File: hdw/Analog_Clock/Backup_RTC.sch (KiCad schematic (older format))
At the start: 4 parts

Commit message: More schematic work
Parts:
- added BT?: CR2032, symbol Device:Battery_Cell
- added BT?: CR2032_Holder, Battery_Holders:Keystone_1058_1x2032-CoinCell, symbol Device:Battery_Cell
- added U?: MIC845N, Package_TO_SOT_SMD:SOT-353_SC-70-5, symbol Comparator:MIC845N
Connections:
- no-connect marks 3 -> 5
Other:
- note added: "REPLACE WITH SOMETHING SIMILAR"
- moved on the sheet: C?, U?
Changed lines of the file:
@@
 EESchema Schematic File Version 4
+LIBS:Analog_Clock-cache
 EELAYER 30 0
 EELAYER END
@@
 L Timer_RTC:DS3231MZ U?
 U 1 1 5E217505
-P 5420 3530
-F 0 "U?" H 5120 3880 50  0000 R CNN
-F 1 "DS3231MZ" H 5870 3880 50  0000 R CNN
-F 2 "Package_SO:SOIC-8_3.9x4.9mm_P1.27mm" H 5420 3030 50  0001 C CNN
-F 3 "http://datasheets.maximintegrated.com/en/ds/DS3231M.pdf" H 5420 2930 50  0001 C CNN
-F 4 "DS3231MZ+-ND" H 5420 3530 50  0001 C CNN "Digi-Key PN"
-	1    5420 3530
+P 5400 2620
+F 0 "U?" H 5100 2970 50  0000 R CNN
+F 1 "DS3231MZ" H 5850 2970 50  0000 R CNN
+F 2 "Package_SO:SOIC-8_3.9x4.9mm_P1.27mm" H 5400 2120 50  0001 C CNN
+F 3 "http://datasheets.maximintegrated.com/en/ds/DS3231M.pdf" H 5400 2020 50  0001 C CNN
+F 4 "DS3231MZ+-ND" H 5400 2620 50  0001 C CNN "Digi-Key PN"
+	1    5400 2620
 	1    0    0    -1
 $EndComp
@@
 L power:GND #PWR?
 U 1 1 5E217898
-P 5420 3930
-F 0 "#PWR?" H 5420 3680 50  0001 C CNN
-F 1 "GND" H 5420 3780 50  0000 C CNN
-F 2 "" H 5420 3930 50  0001 C CNN
-F 3 "" H 5420 3930 50  0001 C CNN
-	1    5420 3930
+P 5400 3020
+F 0 "#PWR?" H 5400 2770 50  0001 C CNN
+F 1 "GND" H 5400 2870 50  0000 C CNN
+F 2 "" H 5400 3020 50  0001 C CNN
+F 3 "" H 5400 3020 50  0001 C CNN
+	1    5400 3020
 	1    0    0    -1
 $EndComp
@@
 L power:+3.3V #PWR?
 U 1 1 5E217DBC
-P 5420 3130
-F 0 "#PWR?" H 5420 2980 50  0001 C CNN
-F 1 "+3.3V" H 5500 3270 50  0000 C CNN
-F 2 "" H 5420 3130 50  0001 C CNN
-F 3 "" H 5420 3130 50  0001 C CNN
-	1    5420 3130
+P 5400 2220
+F 0 "#PWR?" H 5400 2070 50  0001 C CNN
+F 1 "+3.3V" H 5480 2360 50  0000 C CNN
+F 2 "" H 5400 2220 50  0001 C CNN
+F 3 "" H 5400 2220 50  0001 C CNN
+	1    5400 2220
 	1    0    0    -1
 $EndComp
@@
 L Custom_Library:VBAT #PWR?
 U 1 1 5E2180E2
-P 5320 3130
-F 0 "#PWR?" H 5320 2980 50  0001 C CNN
-F 1 "VBAT" H 5240 3270 50  0000 C CNN
-F 2 "" H 5320 3130 50  0001 C CNN
-F 3 "" H 5320 3130 50  0001 C CNN
-	1    5320 3130
-	1    0    0    -1
-$EndComp
-NoConn ~ 5920 3330
-NoConn ~ 5920 3630
-NoConn ~ 4920 3730
-Text GLabel 4920 3430 0    50   BiDi ~ 0
+P 5300 2220
+F 0 "#PWR?" H 5300 2070 50  0001 C CNN
+F 1 "VBAT" H 5220 2360 50  0000 C CNN
+F 2 "" H 5300 2220 50  0001 C CNN
+F 3 "" H 5300 2220 50  0001 C CNN
+	1    5300 2220
+	1    0    0    -1
+$EndComp
+NoConn ~ 5900 2420
+NoConn ~ 5900 2720
+NoConn ~ 4900 2820
+Text GLabel 4900 2520 0    50   BiDi ~ 0
 I2C_SDA
-Text GLabel 4920 3330 0    50   Input ~ 0
+Text GLabel 4900 2420 0    50   Input ~ 0
 I2C_SCL
 $Comp
 L Custom_Library:C_Custom C?
 U 1 1 5E21E9AC
-P 5840 4720
-F 0 "C?" H 5865 4820 50  0000 L CNN
-F 1 "0.1uF" H 5865 4620 50  0000 L CNN
-F 2 "Capacitors_SMD:C_0402" H 5878 4570 50  0001 C CNN
-F 3 "" H 5865 4820 50  0001 C CNN
-F 4 "0402" H 5690 4820 50  0000 R CNN "display_footprint"
-F 5 "50V" H 5690 4720 50  0000 R CNN "Voltage"
-F 6 "X7R" H 5690 4620 50  0000 R CNN "Dielectric"
-F 7 "490-10701-1-ND" H 5840 4720 50  0001 C CNN "Digi-Key PN"
-	1    5840 4720
+P 5820 3810
+F 0 "C?" H 5845 3910 50  0000 L CNN
+F 1 "0.1uF" H 5845 3710 50  0000 L CNN
+F 2 "Capacitors_SMD:C_0402" H 5858 3660 50  0001 C CNN
+F 3 "" H 5845 3910 50  0001 C CNN
+F 4 "0402" H 5670 3910 50  0000 R CNN "display_footprint"
+F 5 "50V" H 5670 3810 50  0000 R CNN "Voltage"
+F 6 "X7R" H 5670 3710 50  0000 R CNN "Dielectric"
+F 7 "490-10701-1-ND" H 5820 3810 50  0001 C CNN "Digi-Key PN"
+	1    5820 3810
 	1    0    0    -1
 $EndComp
@@
 L power:+3.3V #PWR?
 U 1 1 5E21E9B2
-P 5840 4570
-F 0 "#PWR?" H 5840 4420 50  0001 C CNN
-F 1 "+3.3V" H 5840 4710 50  0000 C CNN
-F 2 "" H 5840 4570 50  0000 C CNN
-F 3 "" H 5840 4570 50  0000 C CNN
-	1    5840 4570
+P 5820 3660
+F 0 "#PWR?" H 5820 3510 50  0001 C CNN
+F 1 "+3.3V" H 5820 3800 50  0000 C CNN
+F 2 "" H 5820 3660 50  0000 C CNN
+F 3 "" H 5820 3660 50  0000 C CNN
+	1    5820 3660
 	1    0    0    -1
 $EndComp
@@
 L power:GND #PWR?
 U 1 1 5E21E9B8
-P 5840 4870
-F 0 "#PWR?" H 5840 4620 50  0001 C CNN
-F 1 "GND" H 5840 4720 50  0000 C CNN
-F 2 "" H 5840 4870 50  0001 C CNN
-F 3 "" H 5840 4870 50  0001 C CNN
-	1    5840 4870
+P 5820 3960
+F 0 "#PWR?" H 5820 3710 50  0001 C CNN
+F 1 "GND" H 5820 3810 50  0000 C CNN
+F 2 "" H 5820 3960 50  0001 C CNN
+F 3 "" H 5820 3960 50  0001 C CNN
+	1    5820 3960
 	1    0    0    -1
 $EndComp
@@
 L Custom_Library:C_Custom C?
 U 1 1 5E220EDC
-P 5110 4720
-F 0 "C?" H 5135 4820 50  0000 L CNN
-F 1 "0.1uF" H 5135 4620 50  0000 L CNN
-F 2 "Capacitors_SMD:C_0402" H 5148 4570 50  0001 C CNN
-F 3 "" H 5135 4820 50  0001 C CNN
-F 4 "0402" H 4960 4820 50  0000 R CNN "display_footprint"
-F 5 "50V" H 4960 4720 50  0000 R CNN "Voltage"
-F 6 "X7R" H 4960 4620 50  0000 R CNN "Dielectric"
-F 7 "490-10701-1-ND" H 5110 4720 50  0001 C CNN "Digi-Key PN"
-	1    5110 4720
+P 5090 3810
+F 0 "C?" H 5115 3910 50  0000 L CNN
+F 1 "0.1uF" H 5115 3710 50  0000 L CNN
+F 2 "Capacitors_SMD:C_0402" H 5128 3660 50  0001 C CNN
+F 3 "" H 5115 3910 50  0001 C CNN
+F 4 "0402" H 4940 3910 50  0000 R CNN "display_footprint"
+F 5 "50V" H 4940 3810 50  0000 R CNN "Voltage"
+F 6 "X7R" H 4940 3710 50  0000 R CNN "Dielectric"
+F 7 "490-10701-1-ND" H 5090 3810 50  0001 C CNN "Digi-Key PN"
+	1    5090 3810
 	1    0    0    -1
 $EndComp
@@
 L power:GND #PWR?
 U 1 1 5E220EE8
-P 5110 4870
-F 0 "#PWR?" H 5110 4620 50  0001 C CNN
-F 1 "GND" H 5110 4720 50  0000 C CNN
-F 2 "" H 5110 4870 50  0001 C CNN
-F 3 "" H 5110 4870 50  0001 C CNN
-	1    5110 4870
+P 5090 3960
+F 0 "#PWR?" H 5090 3710 50  0001 C CNN
+F 1 "GND" H 5090 3810 50  0000 C CNN
+F 2 "" H 5090 3960 50  0001 C CNN
+F 3 "" H 5090 3960 50  0001 C CNN
+	1    5090 3960
 	1    0    0    -1
 $EndComp
@@
 L Custom_Library:VBAT #PWR?
 U 1 1 5E220F81
-P 5110 4570
-F 0 "#PWR?" H 5110 4420 50  0001 C CNN
-F 1 "VBAT" H 5110 4720 50  0000 C CNN
-F 2 "" H 5110 4570 50  0001 C CNN
-F 3 "" H 5110 4570 50  0001 C CNN
-	1    5110 4570
+P 5090 3660
+F 0 "#PWR?" H 5090 3510 50  0001 C CNN
+F 1 "VBAT" H 5090 3810 50  0000 C CNN
+F 2 "" H 5090 3660 50  0001 C CNN
+F 3 "" H 5090 3660 50  0001 C CNN
+	1    5090 3660
 	1    0    0    -1
 $EndComp
@@
 L Custom_Library:I2C_Address DOC?
 U 1 1 5E990E17
-P 7180 4080
-F 0 "DOC?" H 7180 4330 60  0001 C CNN
-F 1 "I2C_Address" H 6730 4080 60  0000 L CNN
-F 2 "" H 7180 4430 60  0001 C CNN
-F 3 "" H 7180 4430 60  0001 C CNN
-	1    7180 4080
-	1    0    0    -1
-$EndComp
+P 7160 3170
+F 0 "DOC?" H 7160 3420 60  0001 C CNN
+F 1 "I2C_Address" H 6710 3170 60  0000 L CNN
+F 2 "" H 7160 3520 60  0001 C CNN
+F 3 "" H 7160 3520 60  0001 C CNN
+	1    7160 3170
+	1    0    0    -1
+$EndComp
+$Comp
+L Device:Battery_Cell BT?
+U 1 1 5EA04714
+P 1840 5380
+F 0 "BT?" H 1940 5480 50  0000 L CNN
+F 1 "CR2032" H 1940 5380 50  0000 L CNN
+F 2 "" V 1840 5440 50  0001 C CNN
+F 3 "~" V 1840 5440 50  0001 C CNN
+F 4 "P189-ND" H 1840 5380 50  0001 C CNN "Digi-Key PN"
+	1    1840 5380
+	1    0    0    -1
+$EndComp
+NoConn ~ 1840 5480
+NoConn ~ 1840 5180
+$Comp
+L Device:Battery_Cell BT?
+U 1 1 5EA086C4
+P 2580 5380
+F 0 "BT?" H 2680 5480 50  0000 L CNN
+F 1 "CR2032_Holder" H 2680 5380 50  0000 L CNN
+F 2 "Battery_Holders:Keystone_1058_1x2032-CoinCell" V 2580 5440 50  0001 C CNN
+F 3 "~" V 2580 5440 50  0001 C CNN
+F 4 "36-1058-ND" H 2580 5380 50  0001 C CNN "Digi-Key PN"
+	1    2580 5380
+	1    0    0    -1
+$EndComp
+$Comp
+L power:GND #PWR?
+U 1 1 5EA0966C
+P 2580 5480
+F 0 "#PWR?" H 2580 5230 50  0001 C CNN
+F 1 "GND" H 2580 5330 50  0000 C CNN
+F 2 "" H 2580 5480 50  0001 C CNN
+F 3 "" H 2580 5480 50  0001 C CNN
+	1    2580 5480
+	1    0    0    -1
+$EndComp
+$Comp
+L Custom_Library:VBAT #PWR?
+U 1 1 5EA09B4F
+P 2580 5180
+F 0 "#PWR?" H 2580 5030 50  0001 C CNN
+F 1 "VBAT" H 2580 5330 50  0000 C CNN
+F 2 "" H 2580 5180 50  0001 C CNN
+F 3 "" H 2580 5180 50  0001 C CNN
+	1    2580 5180
+	1    0    0    -1
+$EndComp
+$Comp
+L Comparator:MIC845N U?
+U 1 1 5EA0D285
+P 6230 5620
+F 0 "U?" H 6380 5820 50  0000 C CNN
+F 1 "MIC845N" H 6530 5420 50  0000 C CNN
+F 2 "Package_TO_SOT_SMD:SOT-353_SC-70-5" H 6230 5620 50  0001 C CNN
+F 3 "http://ww1.microchip.com/downloads/en/DeviceDoc/mic845.pdf" H 6380 5820 50  0001 C CNN
+	1    6230 5620
+	1    0    0    -1
+$EndComp
+Text Notes 5780 5640 0    50   ~ 0
+REPLACE WITH SOMETHING SIMILAR
 $EndSCHEMATC

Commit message: More sch work
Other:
- note added: "Replace with smaller battery?"
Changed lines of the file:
@@
 $Descr A 11000 8500
 encoding utf-8
-Sheet 12 20
+Sheet 12 21
 Title ""
 Date ""
@@
 Text Notes 5780 5640 0    50   ~ 0
 REPLACE WITH SOMETHING SIMILAR
+Text Notes 1740 4520 0    100  ~ 20
+Replace with smaller battery?
 $EndSCHEMATC

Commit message: more sch progress
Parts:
- removed U?: MIC845N, Package_TO_SOT_SMD:SOT-353_SC-70-5, symbol Comparator:MIC845N
- added C?: 10uF, Capacitors_SMD:C_0402, symbol Custom_Library:C_Custom
- added R? (x3): 10k, Resistors_SMD:R_0402, symbol Custom_Library:R_Custom
- added R?: 105k, Resistors_SMD:R_0402, symbol Custom_Library:R_Custom
- added U?: TLV6700, TO_SOT_Packages_SMD:TSOT-23-6, symbol Custom_Library:TLV6700
- BT?: value CR2032 -> CR1616; Digi-Key PN P189-ND -> P034-ND
- BT?: value CR2032_Holder -> CR1616_Holder; footprint Battery_Holders:Keystone_1058_1x2032-CoinCell -> Custom Footprints Library:BAT_BU1632SM-JJ-GTR; Digi-Key PN 36-1058-ND -> BU1632SM-JJ-GCT-ND
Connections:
- net labels added: VBAT_PGOOD
- wire segments 0 -> 7
- no-connect marks 5 -> 6
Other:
- note added: "Falling threshold set to 2.5V"
- note removed: "REPLACE WITH SOMETHING SIMILAR"
- note removed: "Replace with smaller battery?"

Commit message: more analog work, added some more sch stuff
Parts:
- removed R? (x2): 10k, Resistors_SMD:R_0402, symbol Custom_Library:R_Custom
- added R?: 10k, Resistors_SMD:R_0402, symbol Custom_Library:R_Custom
- added R?: 22k, Resistors_SMD:R_0603, symbol Custom_Library:R_Custom
- added TP?: TP, Custom Footprints Library:Test_Point, symbol Custom_Library:TP
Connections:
- net GND: now also R?.2, R?.2
- net Backup_RTC_REFCLK: now reaches U?.1 (32KHZ)
- net Backup_RTC_REFCLK: now also R?.1, TP?.1 (TP)
- net at R?.2, U?.3 (+INA): now also R?.1
- no-connect marks 6 -> 5
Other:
- moved on the sheet: BT?, C?, R?, U?

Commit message: big sch push
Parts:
- added C1204, C1205: 0.1uF, Capacitors_SMD:C_0603, symbol Custom_Library:C_Custom
- added R1205, R1206: 562k, Resistors_SMD:R_0603, symbol Custom_Library:R_Custom
- added TP1201: TP, Custom Footprints Library:Test_Point, symbol Custom_Library:TP
- C1201: renamed from C?; footprint Capacitors_SMD:C_0402 -> Capacitors_SMD:C_0603; Digi-Key PN 490-13211-1-ND -> 490-10474-1-ND; Voltage 6.3V -> 10V; display_footprint 0402 -> 0603
- C1202, C1203: renamed from C?; footprint Capacitors_SMD:C_0402 -> Capacitors_SMD:C_0603; Digi-Key PN 490-10701-1-ND -> 399-7845-1-ND; display_footprint 0402 -> 0603
- DOC1201: renamed from DOC?; value I2C_Address -> 0x68
- R1201: renamed from R?; footprint Resistors_SMD:R_0402 -> Resistors_SMD:R_0603; Wattage 1/16W -> 1/10W; display_footprint 0402 -> 0603
- R1202: renamed from R?; Digi-Key PN A129704CT-ND -> (none)
- R1203, R1204: renamed from R?; footprint Resistors_SMD:R_0402 -> Resistors_SMD:R_0603; Digi-Key PN RMCF0402FT10K0CT-ND -> (none); Wattage 1/16W -> 1/10W; display_footprint 0402 -> 0603
- gave numbers to parts that had none: 5
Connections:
- net +3V3: now also C1204.1
- net GND: now also C1204.2, C1205.2, R1206.2
- net VBAT: now also R1205.1, TP1201.1 (TP)
- new net VBAT_ADC: C1205.1, R1205.2, R1206.1
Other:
- moved on the sheet: BT1201, BT1202, C1201, C1202, C1203, R1201, R1202, R1203, R1204, TP1202, U1201, U1202

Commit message: Much more schematic progress
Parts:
- R1201: Digi-Key PN (none) -> RMCF0603FT105KCT-ND
- R1202: Digi-Key PN (none) -> 311-22KLDCT-ND
- R1203, R1204: Digi-Key PN (none) -> YAG2321CT-ND
- R1205, R1206: Digi-Key PN (none) -> 311-562KHRCT-ND
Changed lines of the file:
@@
 encoding utf-8
 Sheet 12 25
-Title ""
-Date ""
-Rev ""
-Comp ""
+Title "Analog Clock"
+Date "2020-08-15"
+Rev "A"
+Comp "Drew Maatman"
 Comment1 ""
 Comment2 ""
@@
 F 5 "1%" H 4200 4390 50  0000 L CNN "Tolerance"
 F 6 "1/10W" H 4200 4320 50  0000 L CNN "Wattage"
+F 7 "RMCF0603FT105KCT-ND" H 4130 4390 50  0001 C CNN "Digi-Key PN"
 	1    4130 4390
 	-1   0    0    -1
@@
 F 5 "1%" H 6280 4390 50  0000 L CNN "Tolerance"
 F 6 "1/10W" H 6280 4320 50  0000 L CNN "Wattage"
-F 7 "" H 6210 4390 50  0001 C CNN "Digi-Key PN"
+F 7 "YAG2321CT-ND" H 6210 4390 50  0001 C CNN "Digi-Key PN"
 	1    6210 4390
 	-1   0    0    -1
@@
 F 5 "1%" H 7990 2030 50  0000 L CNN "Tolerance"
 F 6 "1/10W" H 7990 1960 50  0000 L CNN "Wattage"
-F 7 "" H 7920 2030 50  0001 C CNN "Digi-Key PN"
+F 7 "YAG2321CT-ND" H 7920 2030 50  0001 C CNN "Digi-Key PN"
 	1    7920 2030
 	-1   0    0    -1
@@
 F 5 "1%" H 4200 4810 50  0000 L CNN "Tolerance"
 F 6 "1/10W" H 4200 4720 50  0000 L CNN "Wattage"
-F 7 "" H 4430 5250 60  0001 C CNN "Digi-Key PN"
+F 7 "311-22KLDCT-ND" H 4430 5250 60  0001 C CNN "Digi-Key PN"
 	1    4130 4850
 	-1   0    0    -1
@@
 F 5 "1%" H 8040 4470 50  0000 L CNN "Tolerance"
 F 6 "1/10W" H 8050 4390 50  0000 L CNN "Wattage"
-F 7 "" H 7940 4470 50  0001 C CNN "Digi-Key PN"
+F 7 "311-562KHRCT-ND" H 7940 4470 50  0001 C CNN "Digi-Key PN"
 	1    7940 4470
 	1    0    0    -1
@@
 F 5 "1%" H 8040 4930 50  0000 L CNN "Tolerance"
 F 6 "1/10W" H 8050 4850 50  0000 L CNN "Wattage"
-F 7 "" H 7940 4930 50  0001 C CNN "Digi-Key PN"
+F 7 "311-562KHRCT-ND" H 7940 4930 50  0001 C CNN "Digi-Key PN"
 	1    7940 4930
 	1    0    0    -1

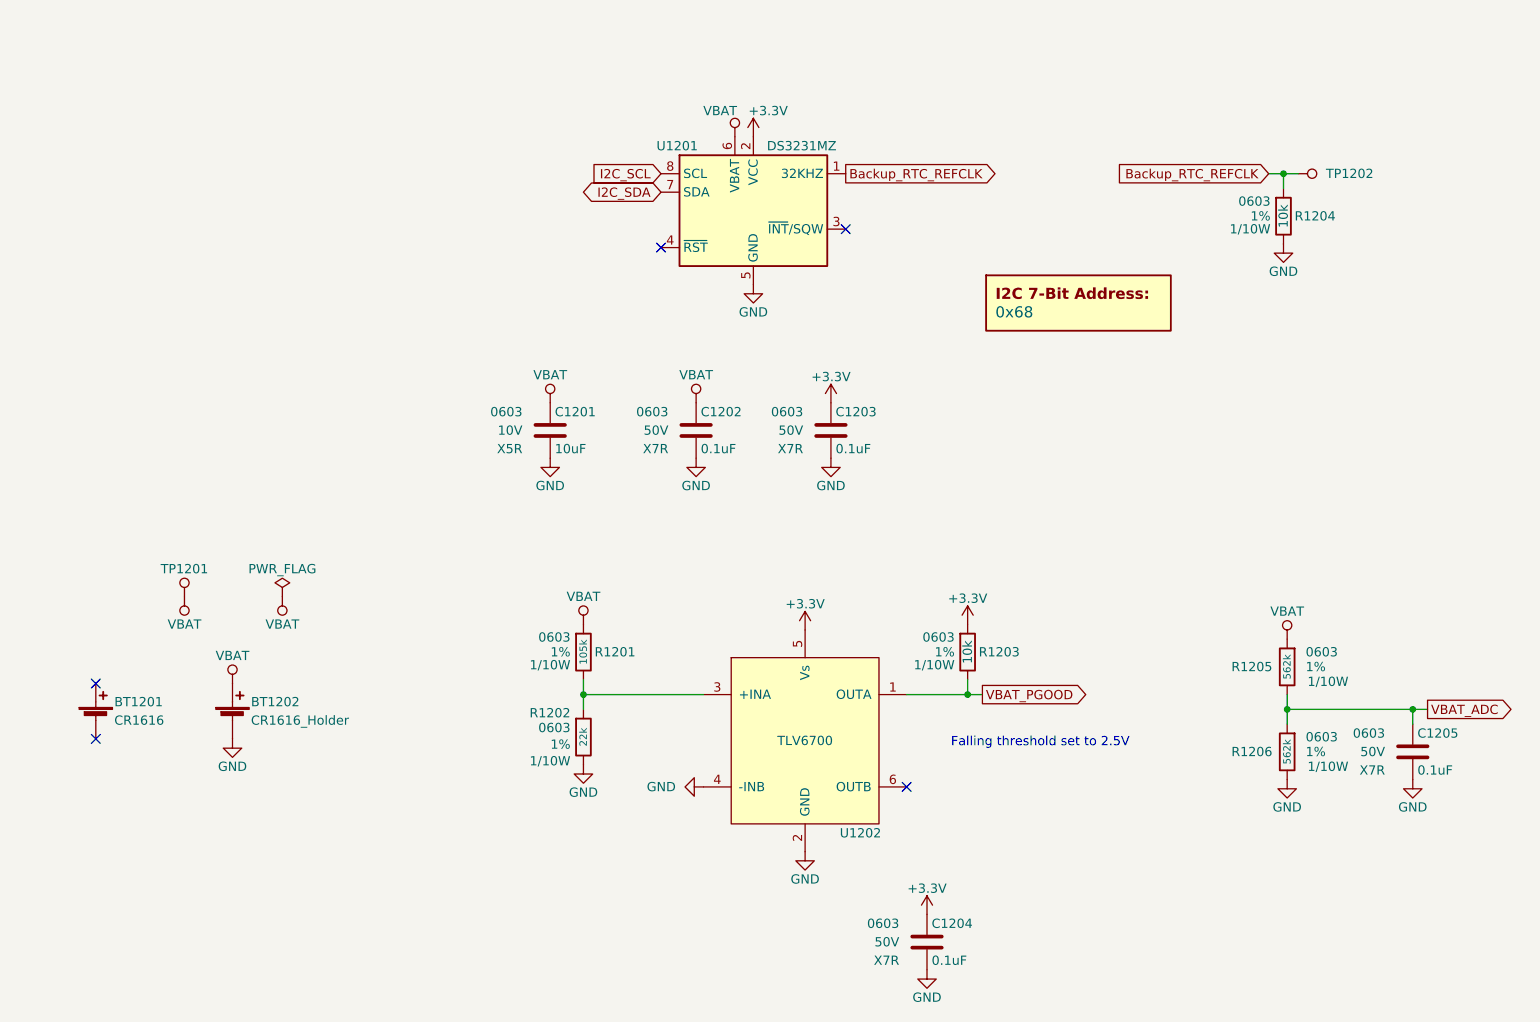
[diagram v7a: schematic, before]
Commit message: Changed VBAT ADC circuit
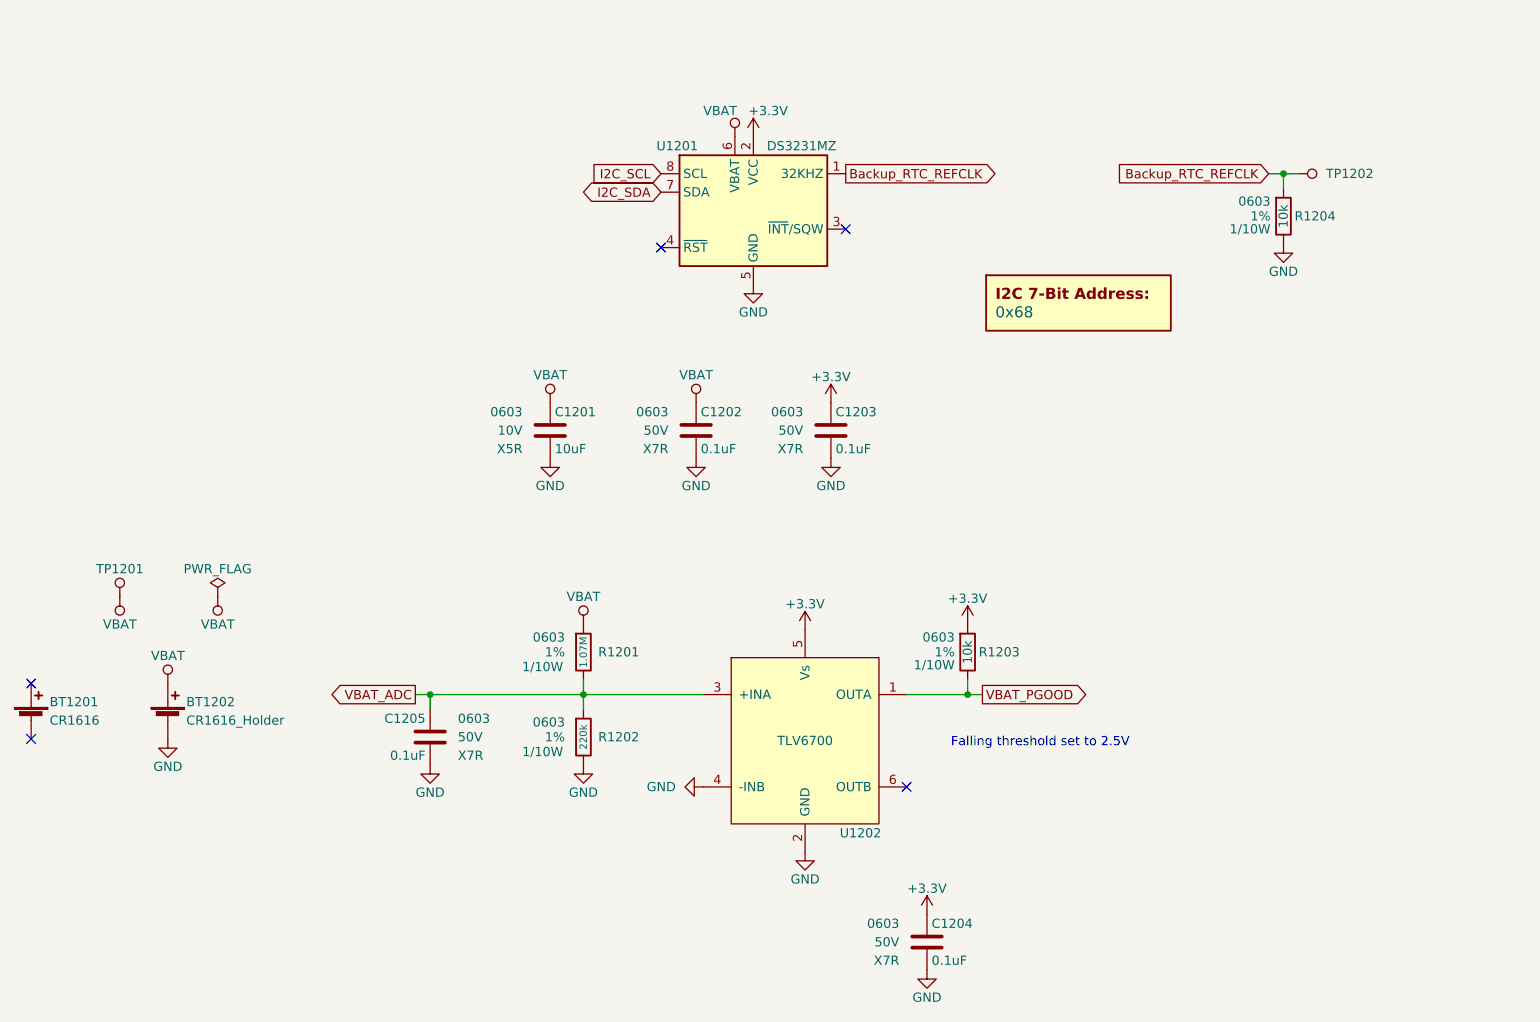
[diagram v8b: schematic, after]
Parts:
- removed R1205, R1206: 562k, Resistors_SMD:R_0603, symbol Custom_Library:R_Custom
- R1201: value 105k -> 1.07M; Digi-Key PN RMCF0603FT105KCT-ND -> RMCF0603FT1M07CT-ND
- R1202: value 22k -> 220k; Digi-Key PN 311-22KLDCT-ND -> RMCF0603FT220KCT-ND
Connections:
- net VBAT_ADC: now also R1201.2, R1202.1, U1202.3 (+INA)
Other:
- moved on the sheet: BT1201, BT1202, C1205, TP1201
